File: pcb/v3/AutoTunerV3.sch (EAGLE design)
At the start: 115 parts, among them IC2 317EMP, U1 TPS63070RNMR

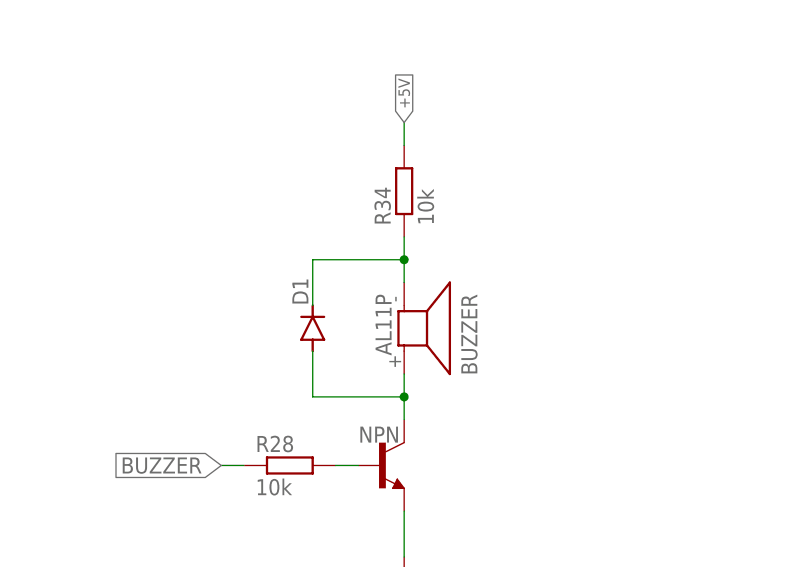
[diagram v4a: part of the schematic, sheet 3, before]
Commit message: critical bat fault & buzzer
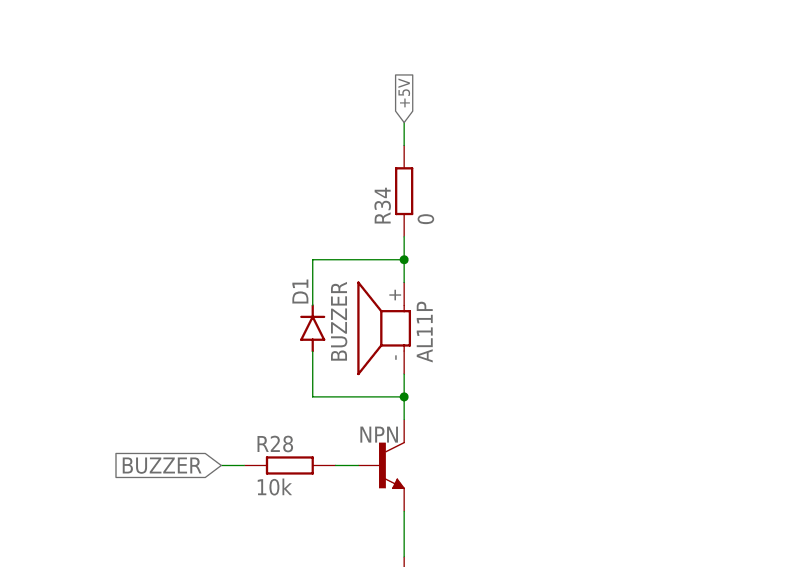
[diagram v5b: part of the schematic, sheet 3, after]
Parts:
- R20: value 330k -> 820k
- R21: value 470k -> 1M
- R34: value 10k -> 0
- R9: value 1M -> 118k
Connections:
- net N$54: now also BUZZER.1; no longer BUZZER.2
- net N$55: now also BUZZER.2; no longer BUZZER.1
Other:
- moved on the sheet: BUZZER
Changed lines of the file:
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@@
 <setting verticaltext="up"/>
 </settings>
-<grid distance="0.1" unitdist="inch" unit="inch" style="dots" multiple="1" display="yes" altdistance="0.01" altunitdist="inch" altunit="inch"/>
+<grid distance="0.1" unitdist="inch" unit="inch" style="lines" multiple="1" display="no" altdistance="0.01" altunitdist="inch" altunit="inch"/>
 <layers>
 <layer number="1" name="Top" color="4" fill="1" visible="no" active="no"/>
@@
 <part name="R17" library="rcl" library_urn="urn:adsk.eagle:library:334" deviceset="R-EU_" device="R0805" package3d_urn="urn:adsk.eagle:package:23553/2" value="0"/>
 <part name="R19" library="rcl" library_urn="urn:adsk.eagle:library:334" deviceset="R-EU_" device="R0805" package3d_urn="urn:adsk.eagle:package:23553/2" value="6k8"/>
-<part name="R9" library="rcl" library_urn="urn:adsk.eagle:library:334" deviceset="R-EU_" device="R0805" package3d_urn="urn:adsk.eagle:package:23553/2" value="1M"/>
+<part name="R9" library="rcl" library_urn="urn:adsk.eagle:library:334" deviceset="R-EU_" device="R0805" package3d_urn="urn:adsk.eagle:package:23553/2" value="118k"/>
 <part name="R10" library="rcl" library_urn="urn:adsk.eagle:library:334" deviceset="R-EU_" device="R0805" package3d_urn="urn:adsk.eagle:package:23553/2" value="1M"/>
-<part name="R20" library="rcl" library_urn="urn:adsk.eagle:library:334" deviceset="R-EU_" device="R0805" package3d_urn="urn:adsk.eagle:package:23553/2" value="330k"/>
-<part name="R21" library="rcl" library_urn="urn:adsk.eagle:library:334" deviceset="R-EU_" device="R0805" package3d_urn="urn:adsk.eagle:package:23553/2" value="470k"/>
+<part name="R20" library="rcl" library_urn="urn:adsk.eagle:library:334" deviceset="R-EU_" device="R0805" package3d_urn="urn:adsk.eagle:package:23553/2" value="820k"/>
+<part name="R21" library="rcl" library_urn="urn:adsk.eagle:library:334" deviceset="R-EU_" device="R0805" package3d_urn="urn:adsk.eagle:package:23553/2" value="1M"/>
 <part name="SCHOTTKY1" library="diode" library_urn="urn:adsk.eagle:library:210" deviceset="DIODE-" device="SOD323-R" package3d_urn="urn:adsk.eagle:package:43437/1">
 <attribute name="LCSC_PART" value="C191023"/>
@@
 </spice>
 </part>
-<part name="R34" library="rcl" library_urn="urn:adsk.eagle:library:334" deviceset="R-EU_" device="R0805" package3d_urn="urn:adsk.eagle:package:23553/2" value="10k">
+<part name="R34" library="rcl" library_urn="urn:adsk.eagle:library:334" deviceset="R-EU_" device="R0805" package3d_urn="urn:adsk.eagle:package:23553/2" value="0">
 <spice>
 <pinmapping spiceprefix="R">
@@
 </spice>
 </part>
-<part name="BUZZER" library="buzzer" library_urn="urn:adsk.eagle:library:113" deviceset="AL11P" device="" package3d_urn="urn:adsk.eagle:package:5308/1"/>
 <part name="GND7" library="supply1" library_urn="urn:adsk.eagle:library:371" deviceset="GND" device=""/>
 <part name="U1" library="TPS63070RNMR" deviceset="TPS63070RNMR" device="">
@@
 </part>
 <part name="JP1" library="pinhead" library_urn="urn:adsk.eagle:library:325" deviceset="PINHD-1X3" device="" package3d_urn="urn:adsk.eagle:package:22458/2"/>
+<part name="BUZZER" library="buzzer" library_urn="urn:adsk.eagle:library:113" deviceset="AL11P" device="" package3d_urn="urn:adsk.eagle:package:5308/1"/>
 </parts>
 <sheets>
@@
 <attribute name="VALUE" x="135.382" y="105.41" size="1.778" layer="96" rot="R90"/>
 </instance>
-<instance part="BUZZER" gate="G$1" x="132.08" y="93.98" smashed="yes" rot="R270">
-<attribute name="NAME" x="138.43" y="97.79" size="1.778" layer="95" rot="R270"/>
-<attribute name="VALUE" x="128.905" y="97.79" size="1.778" layer="96" rot="R270"/>
-</instance>
 <instance part="GND7" gate="1" x="132.08" y="66.04" smashed="yes">
 <attribute name="VALUE" x="129.54" y="63.5" size="1.778" layer="96"/>
@@
 <attribute name="VALUE" x="124.2314" y="96.52" size="1.778" layer="96" rot="R90"/>
 <attribute name="LCSC_PART" x="121.92" y="93.98" size="1.778" layer="96" rot="R90" display="off"/>
+</instance>
+<instance part="BUZZER" gate="G$1" x="132.08" y="93.98" smashed="yes" rot="R90">
+<attribute name="NAME" x="125.73" y="90.17" size="1.778" layer="95" rot="R90"/>
+<attribute name="VALUE" x="135.255" y="90.17" size="1.778" layer="96" rot="R90"/>
 </instance>
 </instances>
@@
 <segment>
 <pinref part="NPN" gate="G$1" pin="C"/>
-<pinref part="BUZZER" gate="G$1" pin="2"/>
 <wire x1="132.08" y1="83.82" x2="132.08" y2="86.36" width="0.1524" layer="91"/>
 <wire x1="132.08" y1="86.36" x2="132.08" y2="88.9" width="0.1524" layer="91"/>
@@
 <pinref part="D1" gate="G$1" pin="A"/>
 <wire x1="121.92" y1="86.36" x2="121.92" y2="91.44" width="0.1524" layer="91"/>
+<pinref part="BUZZER" gate="G$1" pin="1"/>
 </segment>
 </net>
 <net name="N$55" class="0">
 <segment>
-<pinref part="BUZZER" gate="G$1" pin="1"/>
 <pinref part="R34" gate="G$1" pin="1"/>
 <wire x1="132.08" y1="99.06" x2="132.08" y2="101.6" width="0.1524" layer="91"/>
@@
 <wire x1="121.92" y1="101.6" x2="132.08" y2="101.6" width="0.1524" layer="91"/>
 <junction x="132.08" y="101.6"/>
-</segment>
-</net>
+<pinref part="BUZZER" gate="G$1" pin="2"/>
+</segment>
+</net>
